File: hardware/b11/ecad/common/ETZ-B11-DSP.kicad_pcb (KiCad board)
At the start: 2 copper layers, 13.5 x 72.8 mm, 274 parts, among them J1 DSP_CASTELLATED_EDGE

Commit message: Prototype B11 display driver fanout [skip ci]
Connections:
- J1 pad 1: (no net) -> LED_CS29
- J1 pad 10: (no net) -> LED_CS20
- J1 pad 11: (no net) -> LED_CS19
- J1 pad 12: (no net) -> LED_CS18
- J1 pad 13: (no net) -> LED_CS17
- J1 pad 14: (no net) -> LED_CS16
- J1 pad 15: (no net) -> LED_CS15
- J1 pad 16: (no net) -> LED_CS14
- J1 pad 17: (no net) -> LED_CS13
- J1 pad 18: (no net) -> LED_CS12
- J1 pad 19: (no net) -> LED_CS11
- J1 pad 2: (no net) -> LED_CS28
- J1 pad 20: (no net) -> LED_CS10
- J1 pad 21: (no net) -> LED_CS9
- J1 pad 22: (no net) -> LED_CS8
- J1 pad 23: (no net) -> LED_CS7
- J1 pad 24: (no net) -> LED_CS6
- J1 pad 25: (no net) -> LED_CS30
- J1 pad 26: (no net) -> LED_CS31
- J1 pad 27: (no net) -> LED_CS32
- J1 pad 28: (no net) -> LED_CS33
- J1 pad 29: (no net) -> LED_CS34
- J1 pad 3: (no net) -> LED_CS27
- J1 pad 30: (no net) -> LED_CS35
- J1 pad 31: (no net) -> LED_CS36
- J1 pad 32: (no net) -> LED_CS37
- J1 pad 33: (no net) -> LED_CS38
- J1 pad 34: (no net) -> LED_CS39
- J1 pad 37: (no net) -> LED_SW1
- J1 pad 38: (no net) -> LED_SW2
- J1 pad 39: (no net) -> LED_SW3
- J1 pad 4: (no net) -> LED_CS26
- J1 pad 40: (no net) -> LED_SW4
- J1 pad 41: (no net) -> LED_SW5
- J1 pad 42: (no net) -> LED_SW6
- J1 pad 43: (no net) -> LED_SW7
- J1 pad 44: (no net) -> LED_CS1
- J1 pad 45: (no net) -> LED_CS2
- J1 pad 46: (no net) -> LED_CS3
- J1 pad 47: (no net) -> LED_CS4
- J1 pad 48: (no net) -> LED_CS5
- J1 pad 5: (no net) -> LED_CS25
- J1 pad 6: (no net) -> LED_CS24
- J1 pad 7: (no net) -> LED_CS23
- J1 pad 8: (no net) -> LED_CS22
- J1 pad 9: (no net) -> LED_CS21

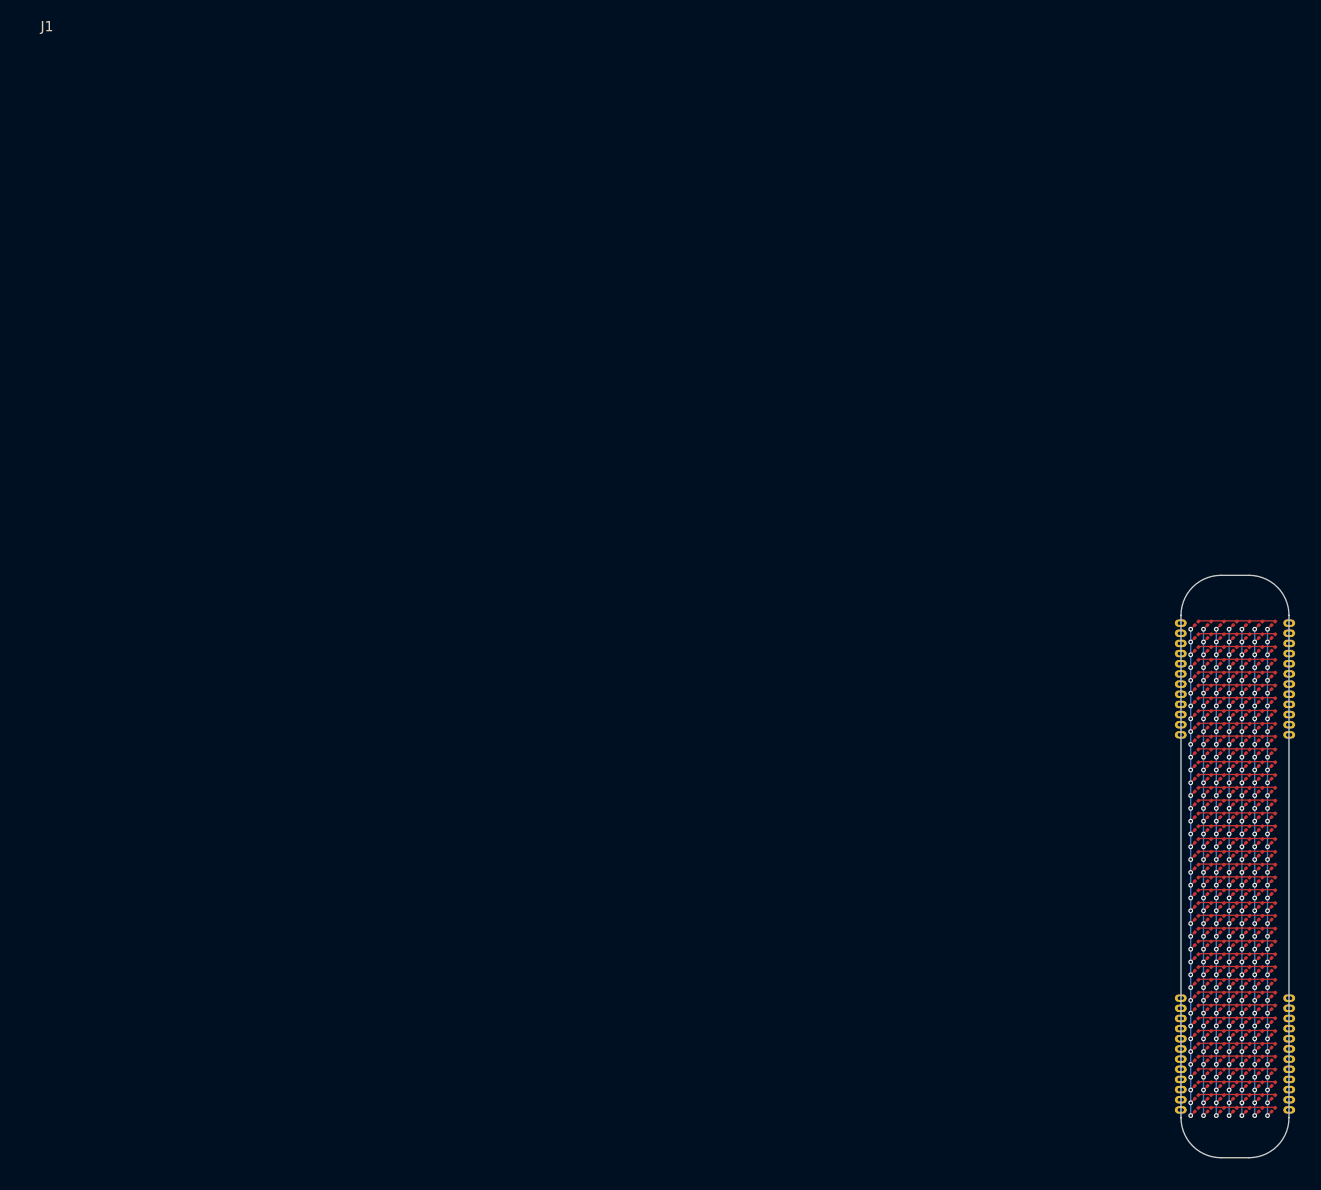
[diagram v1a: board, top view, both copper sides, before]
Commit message: feat: add B11 display module attach footprint [skip ci]
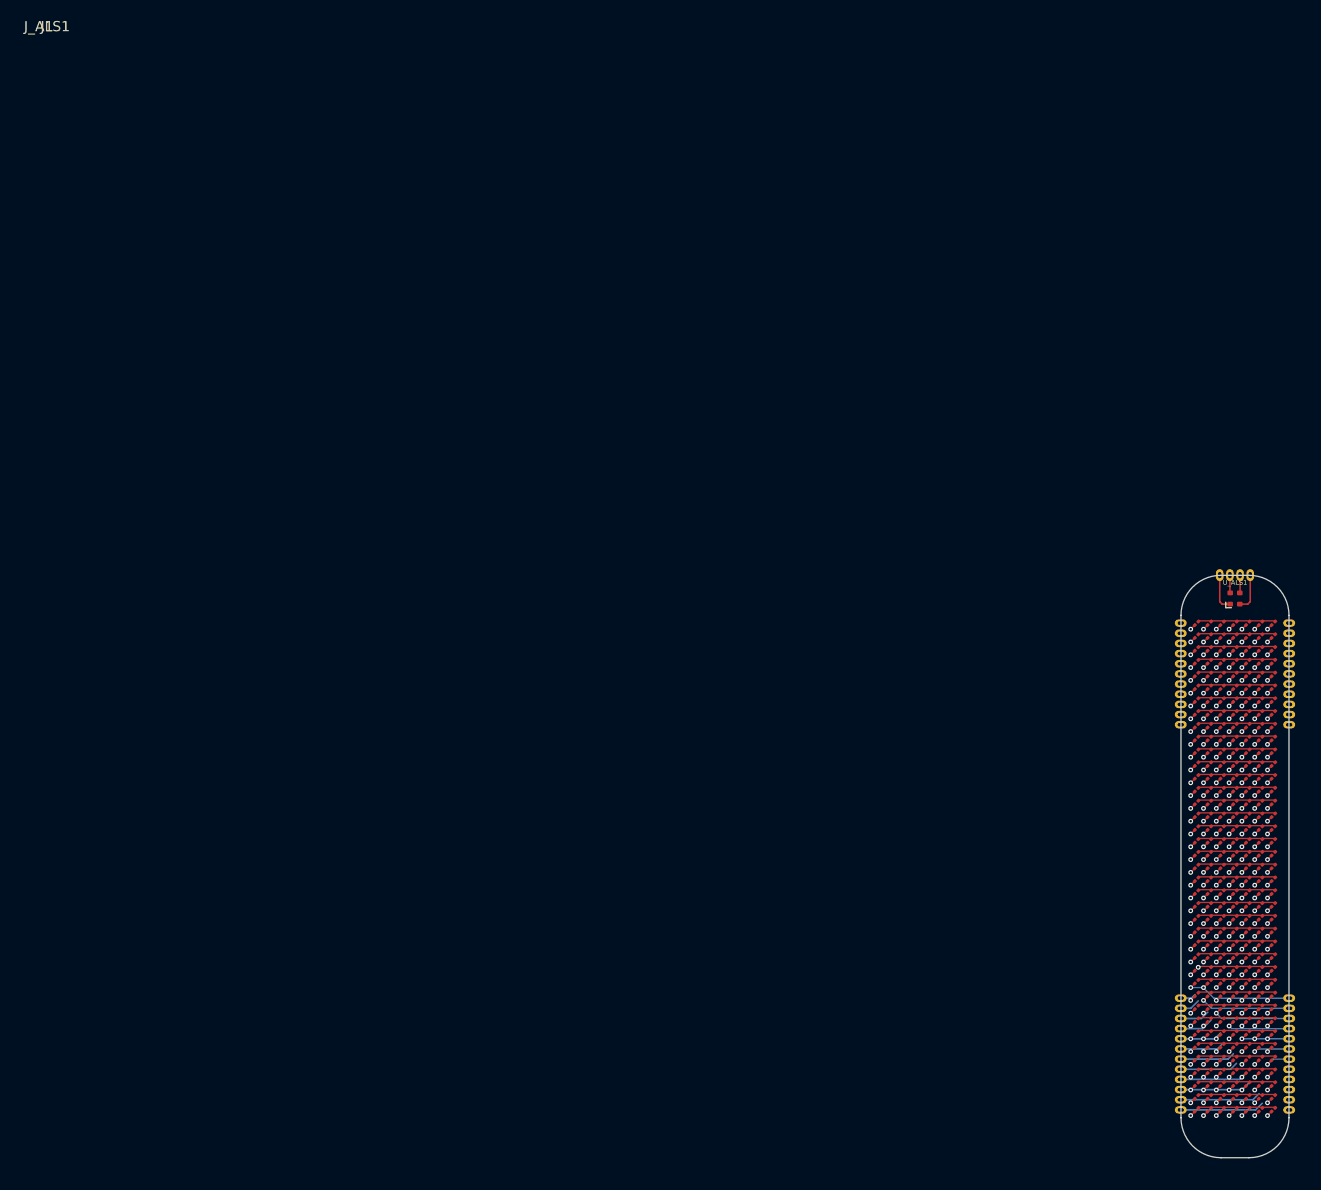
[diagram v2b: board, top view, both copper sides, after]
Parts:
- added J_ALS1: DSP_ALS_CASTELLATIONS, , F.Cu at (0.00, 0.00)
- added U_ALS1: LTR-329ALS-01, LTR-329ALS-01, F.Cu at (148.5, 71.5)
- J1: value DSP_CASTELLATED_EDGE -> DSP_LED_CASTELLATIONS
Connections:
- J1 pad 13: LED_CS17 -> LED_CS16
- J1 pad 14: LED_CS16 -> LED_CS15
- J1 pad 15: LED_CS15 -> LED_CS14
- J1 pad 16: LED_CS14 -> LED_CS13
- J1 pad 17: LED_CS13 -> LED_CS12
- J1 pad 18: LED_CS12 -> LED_CS11
- J1 pad 19: LED_CS11 -> LED_CS10
- J1 pad 20: LED_CS10 -> LED_CS9
- J1 pad 21: LED_CS9 -> LED_CS8
- J1 pad 22: LED_CS8 -> LED_CS7
- J1 pad 23: LED_CS7 -> LED_CS6
- J1 pad 24: LED_CS6 -> LED_CS5
- J1 pad 25: LED_CS30 -> LED_CS4
- J1 pad 26: LED_CS31 -> LED_CS3
- J1 pad 27: LED_CS32 -> LED_CS2
- J1 pad 28: LED_CS33 -> LED_CS1
- J1 pad 29: LED_CS34 -> LED_SW7
- J1 pad 30: LED_CS35 -> LED_SW6
- J1 pad 31: LED_CS36 -> LED_SW5
- J1 pad 32: LED_CS37 -> LED_SW4
- J1 pad 33: LED_CS38 -> LED_SW3
- J1 pad 34: LED_CS39 -> LED_SW2
- J1 pad 35: (no net) -> LED_SW1
- J1 pad 36: (no net) -> LED_CS17
- J1 pad 37: LED_SW1 -> LED_CS39
- J1 pad 38: LED_SW2 -> LED_CS38
- J1 pad 39: LED_SW3 -> LED_CS37
- J1 pad 40: LED_SW4 -> LED_CS36
- J1 pad 41: LED_SW5 -> LED_CS35
- J1 pad 42: LED_SW6 -> LED_CS34
- J1 pad 43: LED_SW7 -> LED_CS33
- J1 pad 44: LED_CS1 -> LED_CS32
- J1 pad 45: LED_CS2 -> LED_CS31
- J1 pad 46: LED_CS3 -> LED_CS30
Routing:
- net (no net): track 0.00 -> 105.6 mm
- net LED_CS28: track 10.2 -> 63.7 mm, vias 0 -> 1
- net LED_CS33: track 10.2 -> 63.3 mm
- net LED_CS35: track 10.2 -> 63.3 mm
- net LED_CS36: track 10.2 -> 62.8 mm
- net LED_CS29: track 10.2 -> 62.5 mm
- net LED_CS34: track 10.2 -> 62.0 mm
- net LED_CS32: track 10.2 -> 61.7 mm
- net LED_CS37: track 10.2 -> 61.6 mm
- net LED_CS31: track 10.2 -> 61.6 mm
- net LED_CS30: track 10.2 -> 61.2 mm
- net LED_CS38: track 10.2 -> 61.1 mm
- net LED_CS39: track 10.2 -> 60.9 mm
- net LED_CS27: track 10.2 -> 56.0 mm
- net LED_CS26: track 10.2 -> 52.7 mm
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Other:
- copper layers 2 -> 4

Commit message: feat: refine B11 display module routing and model [skip ci]
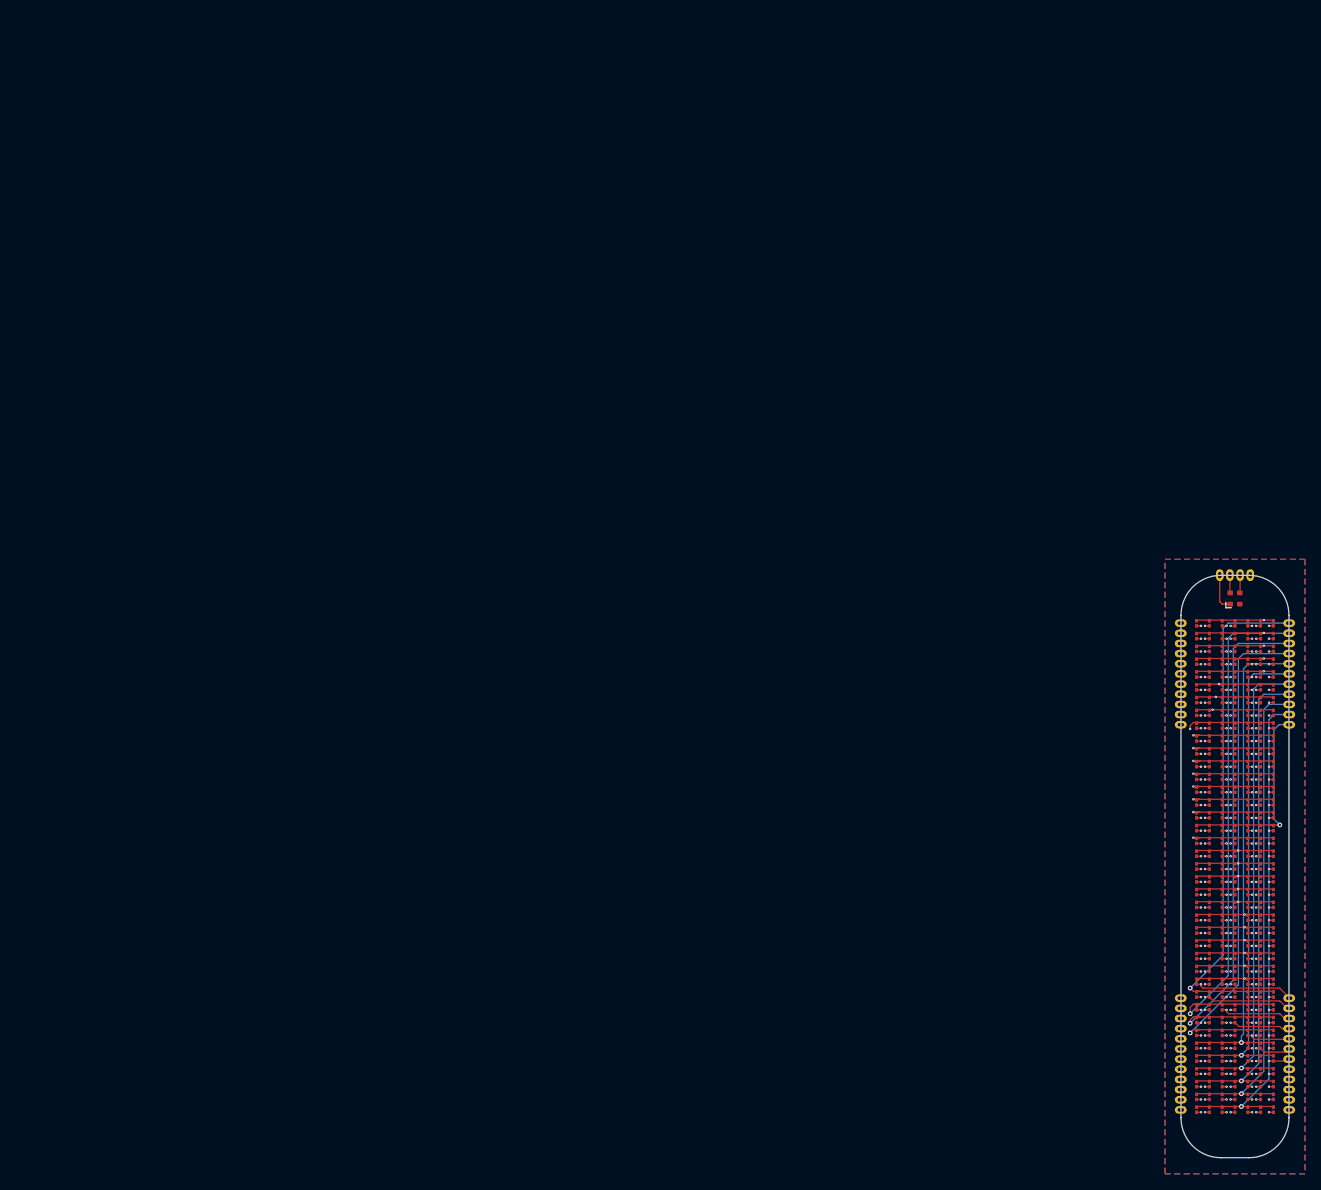
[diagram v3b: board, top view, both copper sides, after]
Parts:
- turned D1 to -90 degrees
- turned D10 to -90 degrees
- turned D100 to -90 degrees
- turned D101 to -90 degrees
- turned D102 to -90 degrees
- turned D103 to -90 degrees
- turned D104 to -90 degrees
- turned D105 to -90 degrees
- turned D106 to -90 degrees
- turned D107 to -90 degrees
- turned D108 to -90 degrees
- turned D109 to -90 degrees
- turned D11 to -90 degrees
- turned D110 to -90 degrees
- turned D111 to -90 degrees
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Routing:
- net (no net): track 105.6 -> 0.00 mm
- net LED_CS1: track 10.2 -> 68.2 mm, vias 0 -> 1
- net LED_CS2: track 10.2 -> 68.0 mm, vias 0 -> 1
- net LED_CS3: track 10.2 -> 67.9 mm, vias 0 -> 1
- net LED_CS4: track 10.2 -> 67.7 mm, vias 0 -> 1
- net LED_CS5: track 10.2 -> 67.5 mm, vias 0 -> 1
- net LED_CS6: track 20.7 -> 67.6 mm, vias 0 -> 1
- net LED_CS7: track 20.2 -> 64.4 mm, vias 0 -> 1
- net LED_CS8: track 19.1 -> 61.3 mm, vias 0 -> 1
- net LED_CS9: track 18.7 -> 60.4 mm, vias 0 -> 1
- net LED_CS10: track 17.4 -> 56.6 mm, vias 0 -> 1
- net LED_CS11: track 17.0 -> 53.4 mm, vias 0 -> 1
- net LED_CS12: track 15.9 -> 50.2 mm, vias 0 -> 1
- net LED_CS13: track 15.4 -> 47.0 mm, vias 0 -> 1
- net LED_CS14: track 14.4 -> 43.7 mm, vias 0 -> 1
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- added copper zone on B.Cu, net ALS_GND
- added copper zone on F.Cu, net ALS_GND
- added copper zone on In1.Cu, net ALS_GND
- added copper zone on In2.Cu, net ALS_GND
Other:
- board text added: "ETZ-B11-DSP"
- board text added: "Rev A"
- board text added: "V1.0.0"
